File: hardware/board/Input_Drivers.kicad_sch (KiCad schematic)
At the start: 14 parts

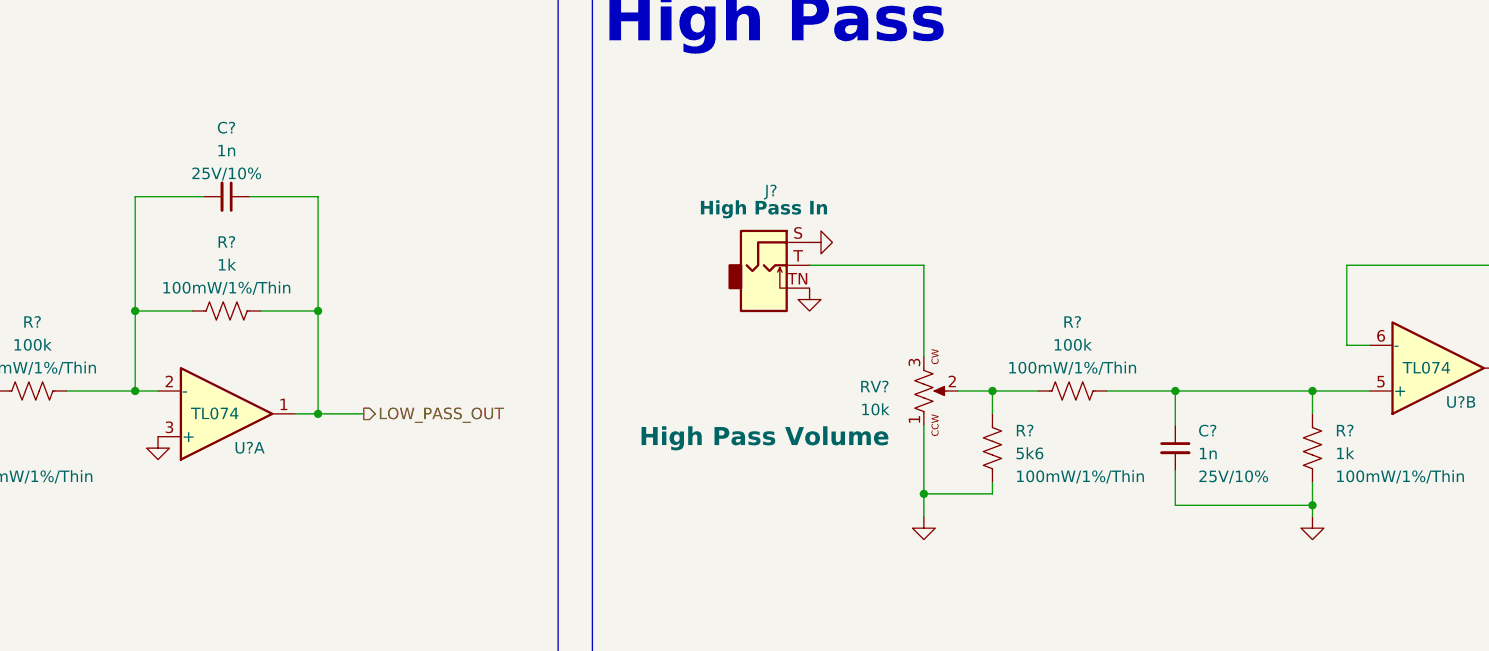
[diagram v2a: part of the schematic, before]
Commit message: hardware: add MPNs, DigiKey part numbers, and LCSC part numbers for all BOM items
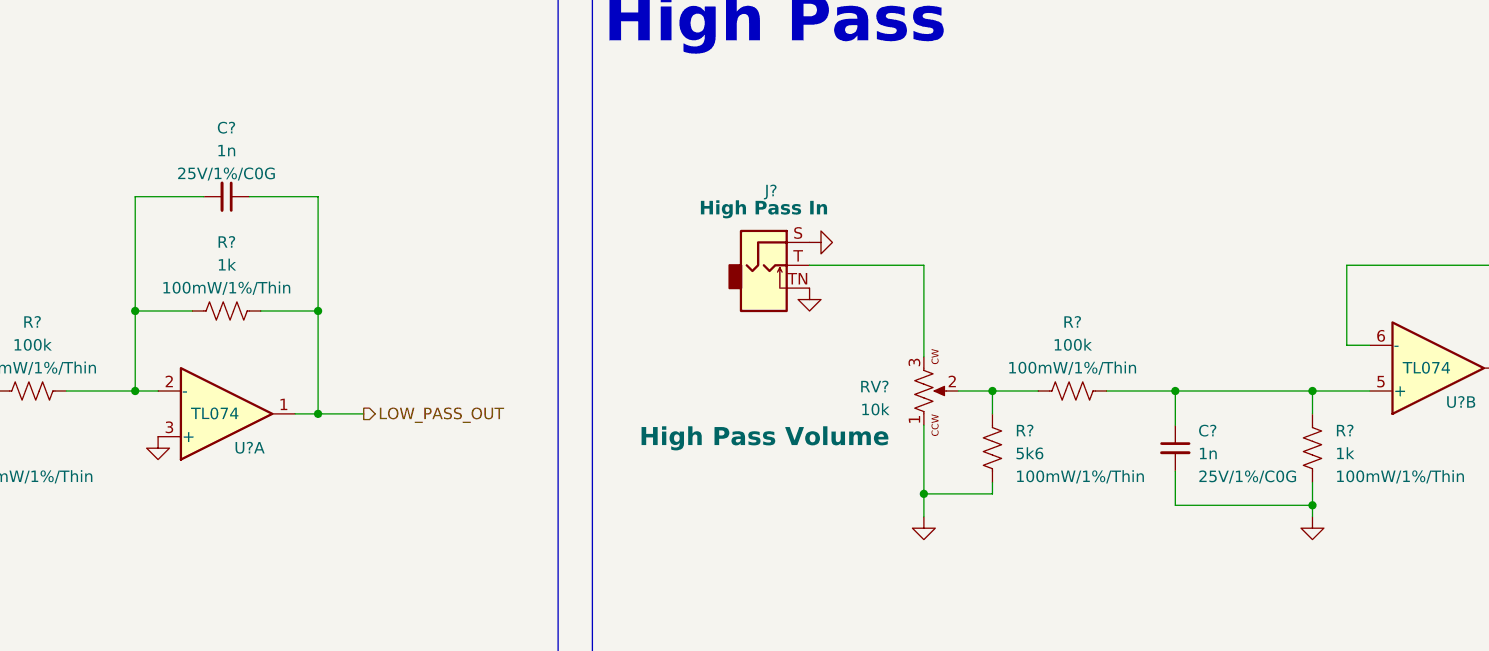
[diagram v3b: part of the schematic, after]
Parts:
- C? (x2): DigiKey (none) -> 490-GCM1885C2A102FA16DCT-ND; LCSC (none) -> C2219251; MPN (none) -> GCM1885C2A102FA16D; Rating 25V/10% -> 25V/1%/C0G; Substitutes Allowed (none) -> Ask
- R? (x2): DigiKey (none) -> YAG2323TR-ND; LCSC (none) -> C375503; MPN (none) -> RT0603FRE071KL; Substitutes Allowed (none) -> Yes
- R? (x2): DigiKey (none) -> 13-RT0603FRE075K6LCT-ND; LCSC (none) -> C706186; MPN (none) -> RT0603FRE075K6L; Substitutes Allowed (none) -> Yes
- R? (x2): DigiKey (none) -> 13-RT0603FRE13100KLTR-ND; LCSC (none) -> C4107493; MPN (none) -> RT0603FRE13100KL; Substitutes Allowed (none) -> Yes
- U? (x2): DigiKey (none) -> 296-7198-1-ND; LCSC (none) -> C96507; MPN TL074CPW -> TL074CPWR; Substitutes Allowed (none) -> No
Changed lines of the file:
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@@
       (effects (font (size 1.27 1.27)) hide)
     )
-    (property "MPN" "TL074CPW" (at 93.98 116.84 0)
+    (property "MPN" "TL074CPWR" (at 93.98 116.84 0)
+      (effects (font (size 1.27 1.27)) hide)
+    )
+    (property "DigiKey" "296-7198-1-ND" (at 93.98 109.22 0)
+      (effects (font (size 1.27 1.27)) hide)
+    )
+    (property "LCSC" "C96507" (at 93.98 109.22 0)
+      (effects (font (size 1.27 1.27)) hide)
+    )
+    (property "Substitutes Allowed" "No" (at 93.98 109.22 0)
       (effects (font (size 1.27 1.27)) hide)
     )
@@
       (effects (font (size 1.27 1.27)) hide)
     )
-    (property "MPN" "TL074CPW" (at 228.6 111.76 0)
+    (property "MPN" "TL074CPWR" (at 228.6 111.76 0)
+      (effects (font (size 1.27 1.27)) hide)
+    )
+    (property "DigiKey" "296-7198-1-ND" (at 228.6 104.14 0)
+      (effects (font (size 1.27 1.27)) hide)
+    )
+    (property "LCSC" "C96507" (at 228.6 104.14 0)
+      (effects (font (size 1.27 1.27)) hide)
+    )
+    (property "Substitutes Allowed" "No" (at 228.6 104.14 0)
       (effects (font (size 1.27 1.27)) hide)
     )
@@
       (effects (font (size 1.27 1.27)) hide)
     )
-    (property "Rating" "25V/10%" (at 93.9736 82.55 90)
-      (effects (font (size 1.27 1.27)))
+    (property "Rating" "25V/1%/C0G" (at 93.9736 82.55 90)
+      (effects (font (size 1.27 1.27)))
+    )
+    (property "DigiKey" "490-GCM1885C2A102FA16DCT-ND" (at 93.98 85.09 0)
+      (effects (font (size 1.27 1.27)) hide)
+    )
+    (property "LCSC" "C2219251" (at 93.98 85.09 0)
+      (effects (font (size 1.27 1.27)) hide)
+    )
+    (property "MPN" "GCM1885C2A102FA16D" (at 93.98 85.09 0)
+      (effects (font (size 1.27 1.27)) hide)
+    )
+    (property "Substitutes Allowed" "Ask" (at 93.98 85.09 0)
+      (effects (font (size 1.27 1.27)) hide)
     )
     (pin "1")
@@
     (property "Rating" "100mW/1%/Thin" (at 93.98 95.25 90)
       (effects (font (size 1.27 1.27)))
+    )
+    (property "DigiKey" "YAG2323TR-ND" (at 93.98 97.79 0)
+      (effects (font (size 1.27 1.27)) hide)
+    )
+    (property "LCSC" "C375503" (at 93.98 97.79 0)
+      (effects (font (size 1.27 1.27)) hide)
+    )
+    (property "Substitutes Allowed" "Yes" (at 93.98 97.79 0)
+      (effects (font (size 1.27 1.27)) hide)
+    )
+    (property "MPN" "RT0603FRE071KL" (at 93.98 97.79 0)
+      (effects (font (size 1.27 1.27)) hide)
     )
     (pin "1")
@@
       (effects (font (size 2 2) bold) (justify left))
     )
+    (property "DigiKey" "" (at 171.45 106.68 0)
+      (effects (font (size 1.27 1.27)) hide)
+    )
+    (property "LCSC" "" (at 171.45 106.68 0)
+      (effects (font (size 1.27 1.27)) hide)
+    )
+    (property "Substitutes Allowed" "" (at 171.45 106.68 0)
+      (effects (font (size 1.27 1.27)) hide)
+    )
     (pin "1")
     (pin "2")
@@
       (effects (font (size 1.27 1.27)) hide)
     )
-    (property "Rating" "25V/10%" (at 201.93 116.2113 0)
-      (effects (font (size 1.27 1.27)) (justify left))
+    (property "Rating" "25V/1%/C0G" (at 201.93 116.2113 0)
+      (effects (font (size 1.27 1.27)) (justify left))
+    )
+    (property "DigiKey" "490-GCM1885C2A102FA16DCT-ND" (at 199.39 113.03 0)
+      (effects (font (size 1.27 1.27)) hide)
+    )
+    (property "LCSC" "C2219251" (at 199.39 113.03 0)
+      (effects (font (size 1.27 1.27)) hide)
+    )
+    (property "MPN" "GCM1885C2A102FA16D" (at 199.39 113.03 0)
+      (effects (font (size 1.27 1.27)) hide)
+    )
+    (property "Substitutes Allowed" "Ask" (at 199.39 113.03 0)
+      (effects (font (size 1.27 1.27)) hide)
     )
     (pin "1")
@@
       (effects (font (size 1.5 1.5) bold))
     )
+    (property "DigiKey" "" (at 153.67 93.98 0)
+      (effects (font (size 1.27 1.27)) hide)
+    )
+    (property "LCSC" "" (at 153.67 93.98 0)
+      (effects (font (size 1.27 1.27)) hide)
+    )
+    (property "Substitutes Allowed" "" (at 153.67 93.98 0)
+      (effects (font (size 1.27 1.27)) hide)
+    )
     (pin "S")
     (pin "T")
@@
       (effects (font (size 1.27 1.27)) (justify left))
     )
+    (property "DigiKey" "13-RT0603FRE075K6LCT-ND" (at 179.07 113.03 0)
+      (effects (font (size 1.27 1.27)) hide)
+    )
+    (property "LCSC" "C706186" (at 179.07 113.03 0)
+      (effects (font (size 1.27 1.27)) hide)
+    )
+    (property "Substitutes Allowed" "Yes" (at 179.07 113.03 0)
+      (effects (font (size 1.27 1.27)) hide)
+    )
+    (property "MPN" "RT0603FRE075K6L" (at 179.07 113.03 0)
+      (effects (font (size 1.27 1.27)) hide)
+    )
     (pin "1")
     (pin "2")
@@
       (effects (font (size 1.27 1.27)))
     )
+    (property "DigiKey" "13-RT0603FRE13100KLTR-ND" (at 187.96 106.68 0)
+      (effects (font (size 1.27 1.27)) hide)
+    )
+    (property "LCSC" "C4107493" (at 187.96 106.68 0)
+      (effects (font (size 1.27 1.27)) hide)
+    )
+    (property "Substitutes Allowed" "Yes" (at 187.96 106.68 0)
+      (effects (font (size 1.27 1.27)) hide)
+    )
+    (property "MPN" "RT0603FRE13100KL" (at 187.96 106.68 0)
+      (effects (font (size 1.27 1.27)) hide)
+    )
     (pin "1")
     (pin "2")
@@
       (effects (font (size 1.27 1.27)))
     )
+    (property "DigiKey" "13-RT0603FRE13100KLTR-ND" (at 72.39 106.68 0)
+      (effects (font (size 1.27 1.27)) hide)
+    )
+    (property "LCSC" "C4107493" (at 72.39 106.68 0)
+      (effects (font (size 1.27 1.27)) hide)
+    )
+    (property "Substitutes Allowed" "Yes" (at 72.39 106.68 0)
+      (effects (font (size 1.27 1.27)) hide)
+    )
+    (property "MPN" "RT0603FRE13100KL" (at 72.39 106.68 0)
+      (effects (font (size 1.27 1.27)) hide)
+    )
     (pin "1")
     (pin "2")
@@
       (effects (font (size 1.27 1.27)) (justify left))
     )
+    (property "DigiKey" "YAG2323TR-ND" (at 214.63 113.03 0)
+      (effects (font (size 1.27 1.27)) hide)
+    )
+    (property "LCSC" "C375503" (at 214.63 113.03 0)
+      (effects (font (size 1.27 1.27)) hide)
+    )
+    (property "Substitutes Allowed" "Yes" (at 214.63 113.03 0)
+      (effects (font (size 1.27 1.27)) hide)
+    )
+    (property "MPN" "RT0603FRE071KL" (at 214.63 113.03 0)
+      (effects (font (size 1.27 1.27)) hide)
+    )
     (pin "1")
     (pin "2")
@@
     (property "Rating" "100mW/1%/Thin" (at 64.77 116.205 0)
       (effects (font (size 1.27 1.27)) (justify left))
+    )
+    (property "DigiKey" "13-RT0603FRE075K6LCT-ND" (at 62.23 113.03 0)
+      (effects (font (size 1.27 1.27)) hide)
+    )
+    (property "LCSC" "C706186" (at 62.23 113.03 0)
+      (effects (font (size 1.27 1.27)) hide)
+    )
+    (property "Substitutes Allowed" "Yes" (at 62.23 113.03 0)
+      (effects (font (size 1.27 1.27)) hide)
+    )
+    (property "MPN" "RT0603FRE075K6L" (at 62.23 113.03 0)
+      (effects (font (size 1.27 1.27)) hide)
     )
     (pin "1")
@@
       (effects (font (size 2 2) bold) (justify left))
     )
+    (property "DigiKey" "" (at 54.61 106.68 0)
+      (effects (font (size 1.27 1.27)) hide)
+    )
+    (property "LCSC" "" (at 54.61 106.68 0)
+      (effects (font (size 1.27 1.27)) hide)
+    )
+    (property "Substitutes Allowed" "" (at 54.61 106.68 0)
+      (effects (font (size 1.27 1.27)) hide)
+    )
     (pin "1")
     (pin "2")
@@
       (effects (font (size 1.5 1.5) bold))
     )
+    (property "DigiKey" "" (at 36.83 93.98 0)
+      (effects (font (size 1.27 1.27)) hide)
+    )
+    (property "LCSC" "" (at 36.83 93.98 0)
+      (effects (font (size 1.27 1.27)) hide)
+    )
+    (property "Substitutes Allowed" "" (at 36.83 93.98 0)
+      (effects (font (size 1.27 1.27)) hide)
+    )
     (pin "S")

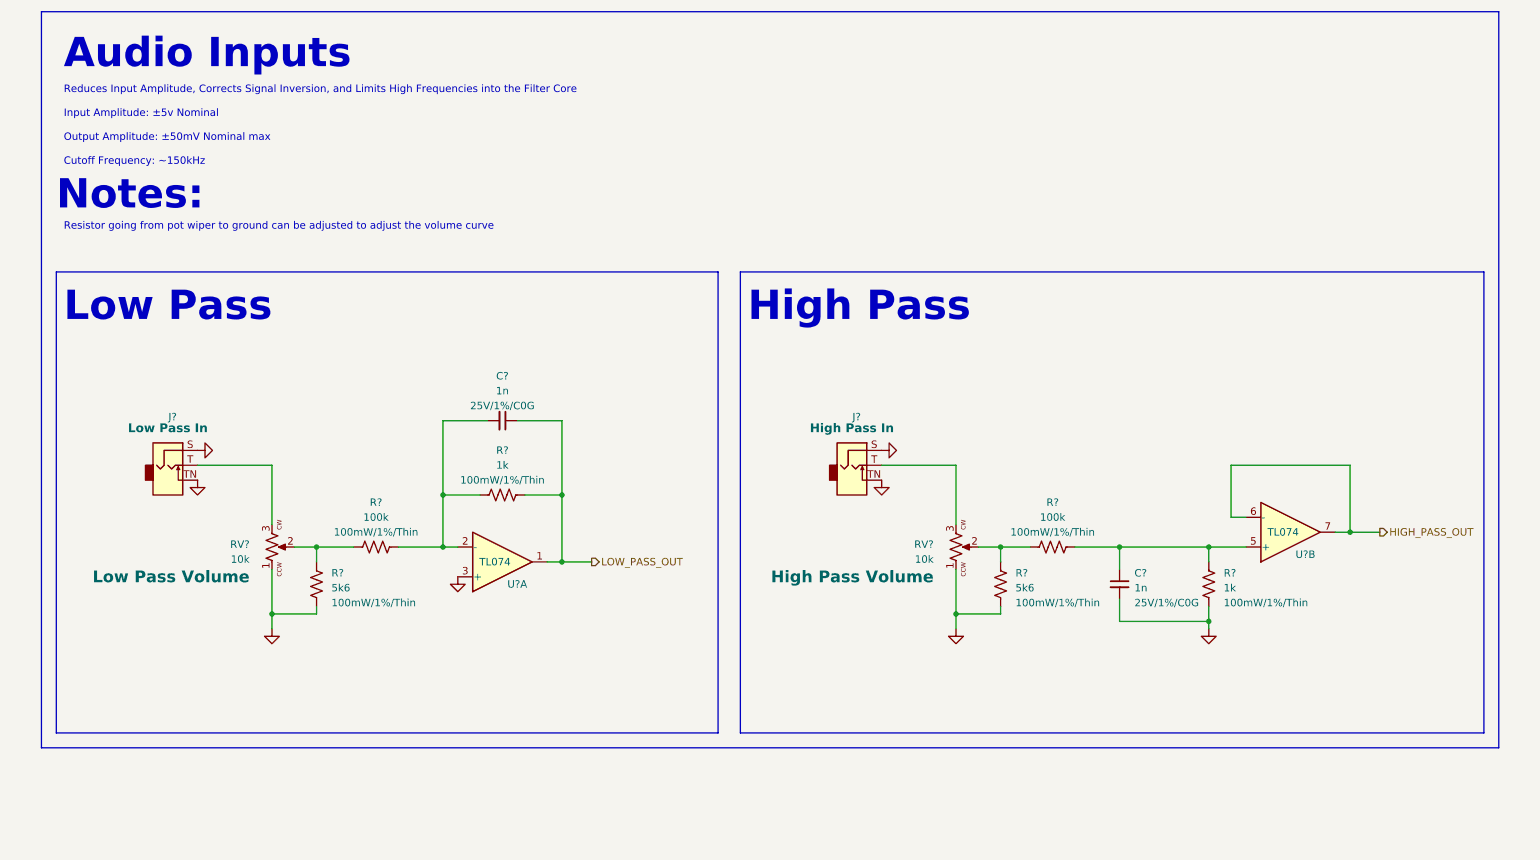
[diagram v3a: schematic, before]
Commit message: hardware: update schematic fonts/text sizes, some slight readability improvements
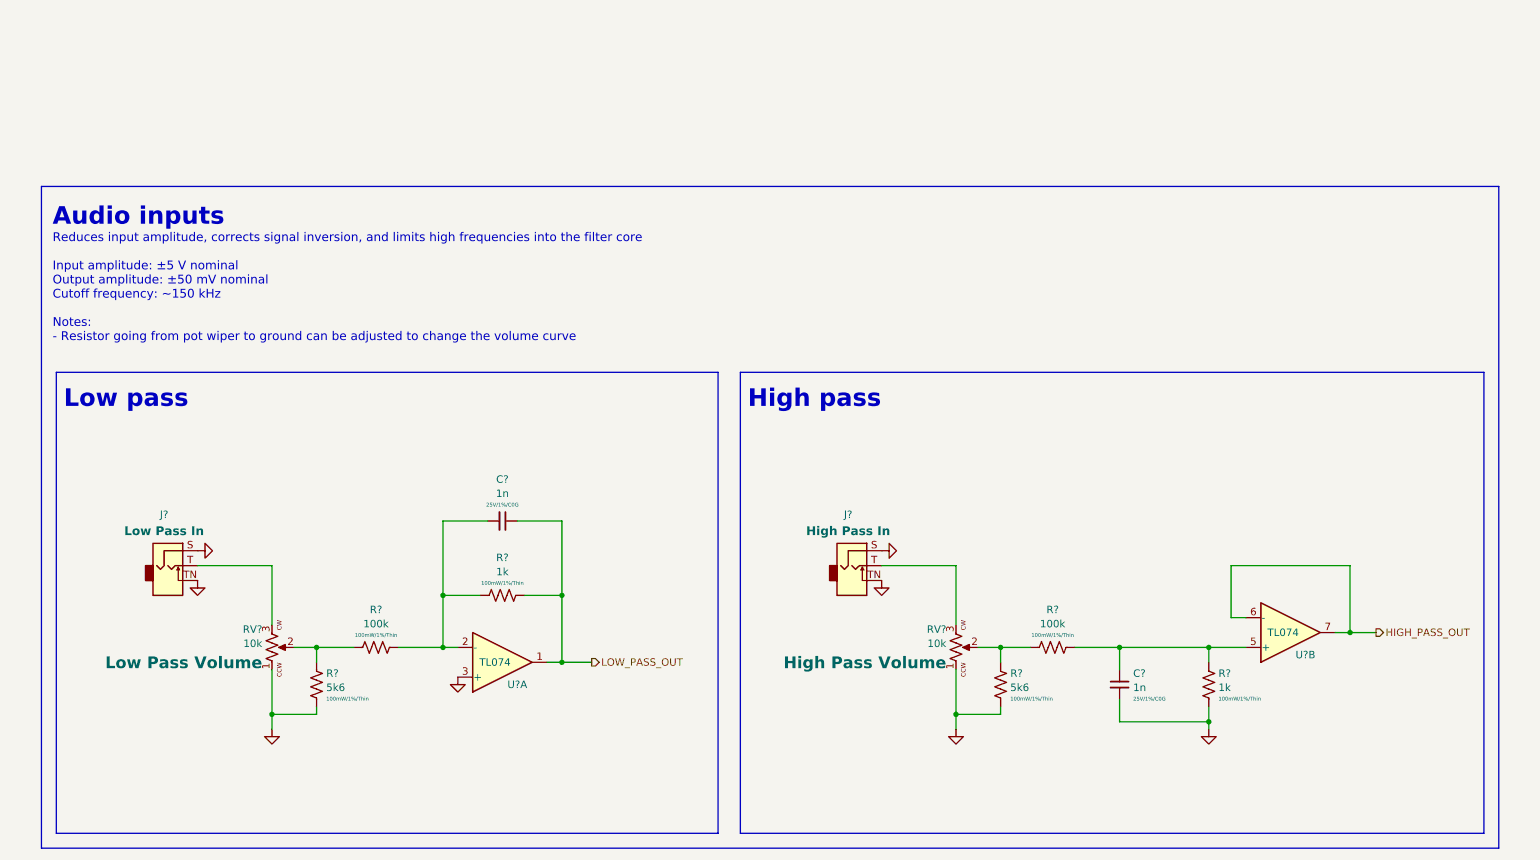
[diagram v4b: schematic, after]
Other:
- note added: "Audio inputs"
- note added: "High pass"
- note added: "Low pass"
- note added: "Reduces input amplitude, corrects signal inversion, and limits high frequencies into the filter core Input amplitude: ±5 V nominal Output amplitude: ±50 mV nominal Cutoff frequency: ~150 kHz Notes: - Resistor going from pot wiper to ground can be adjusted to change the volume curve"
- note removed: "Audio Inputs"
- note removed: "High Pass"
- note removed: "Low Pass"
- note removed: "Notes:"
- note removed: "Reduces Input Amplitude, Corrects Signal Inversion, and Limits High Frequencies into the Filter Core Input Amplitude: ±5v Nominal Output Amplitude: ±50mV Nominal max Cutoff Frequency: ~150kHz"
- note removed: "Resistor going from pot wiper to ground can be adjusted to adjust the volume curve"
- moved on the sheet: C?, J?, R?, RV?, U?A, U?B

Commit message: hardware: use new Winterbloom sheet layout
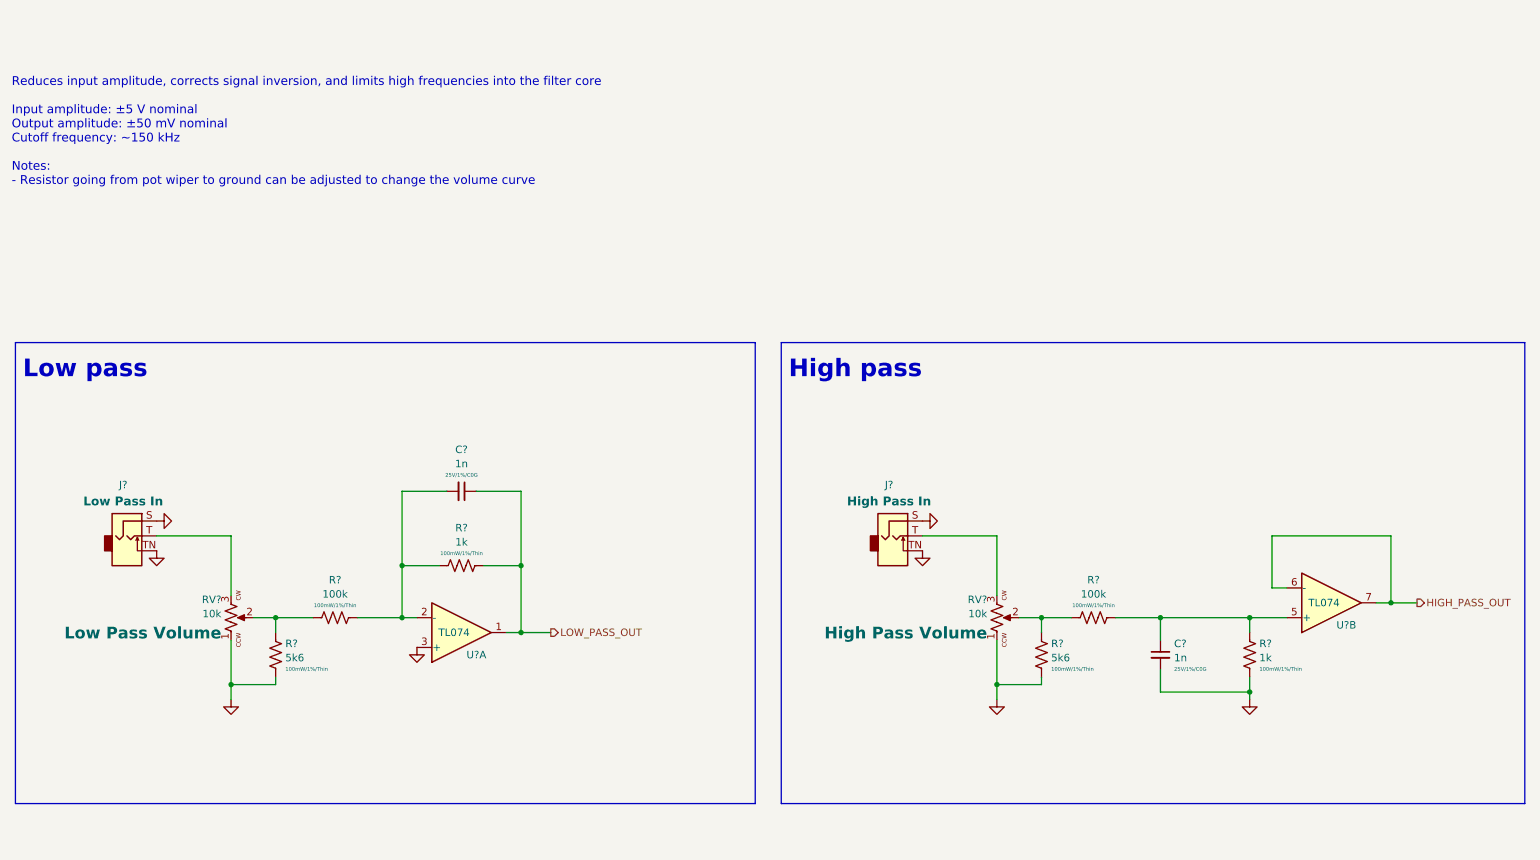
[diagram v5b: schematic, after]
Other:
- note removed: "Audio inputs"
- moved on the sheet: C?, J?, R?, RV?, U?A, U?B
